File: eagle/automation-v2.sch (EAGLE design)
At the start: 103 parts, among them IC1 MEGA48/88/168-AU, IC2 DS2482-100S, IC3 DS2482-100S, IC4 78L33, K1 SRD-05VDC-SL-C, K2 SRD-05VDC-SL-C, K3 SRD-05VDC-SL-C, K4 SRD-05VDC-SL-C, Q1 BSS123, Q2 BSS123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

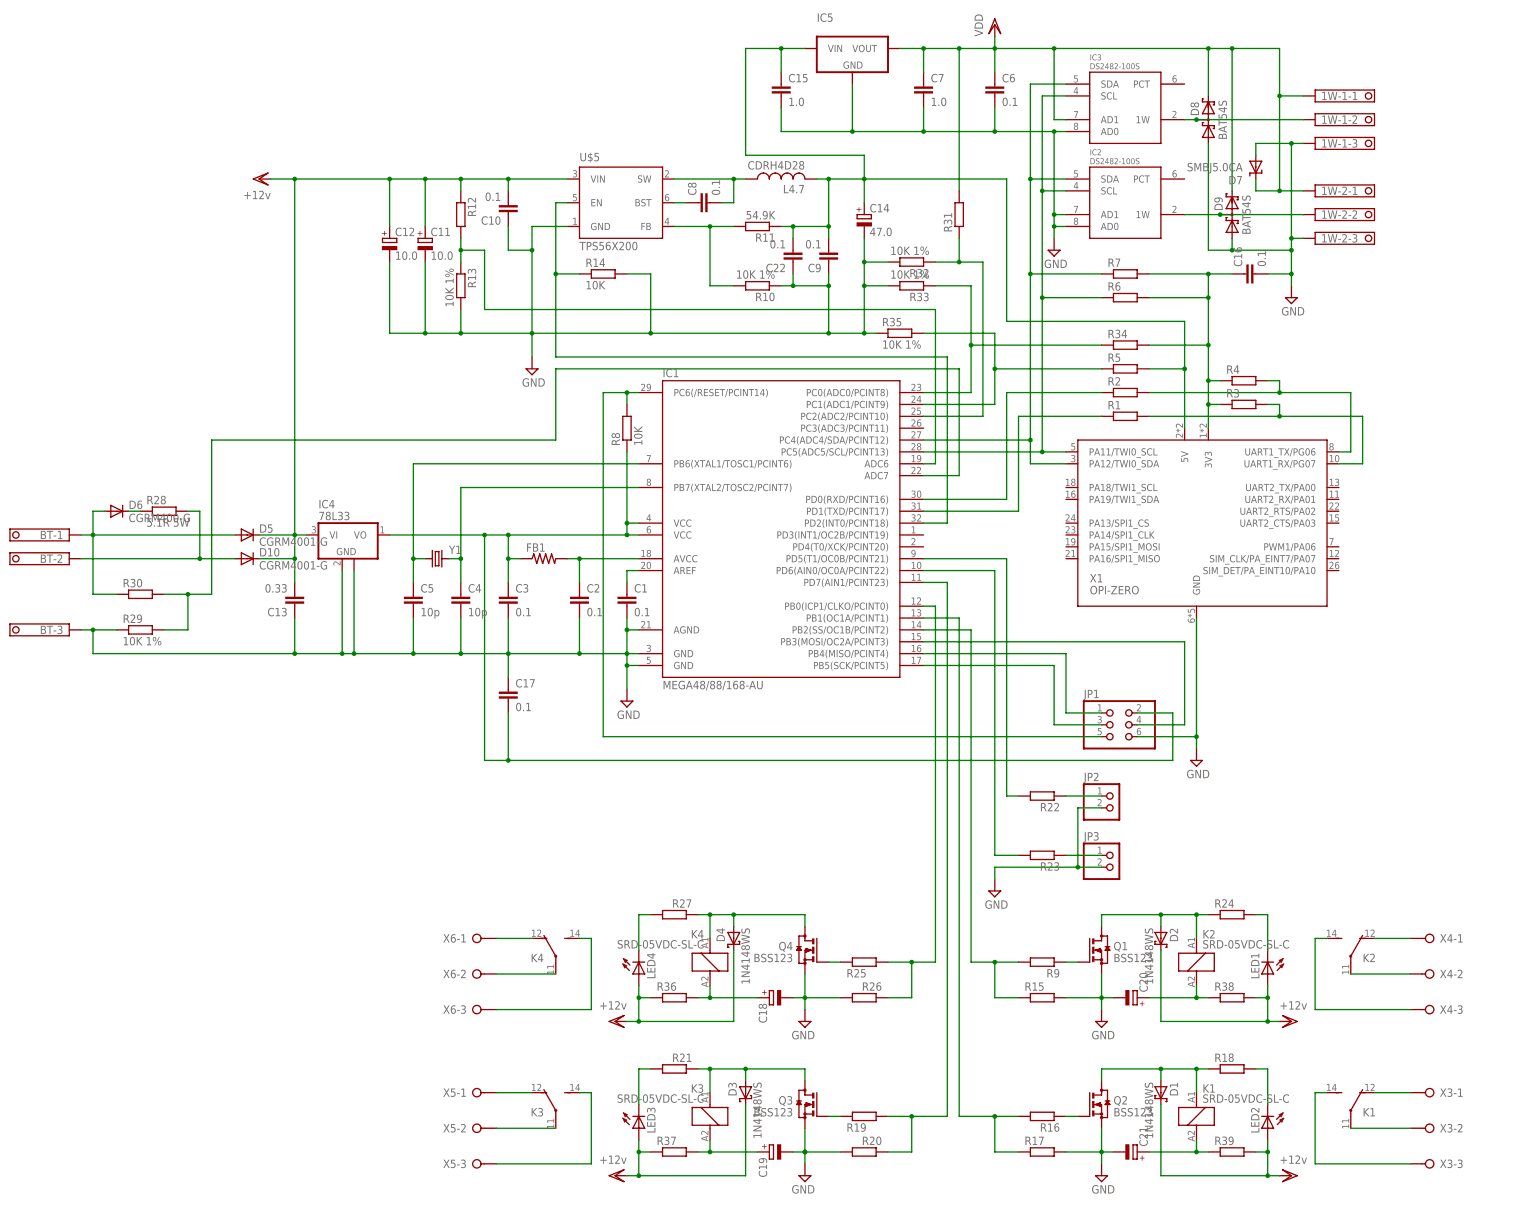
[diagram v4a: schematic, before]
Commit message: changed Relay footprint
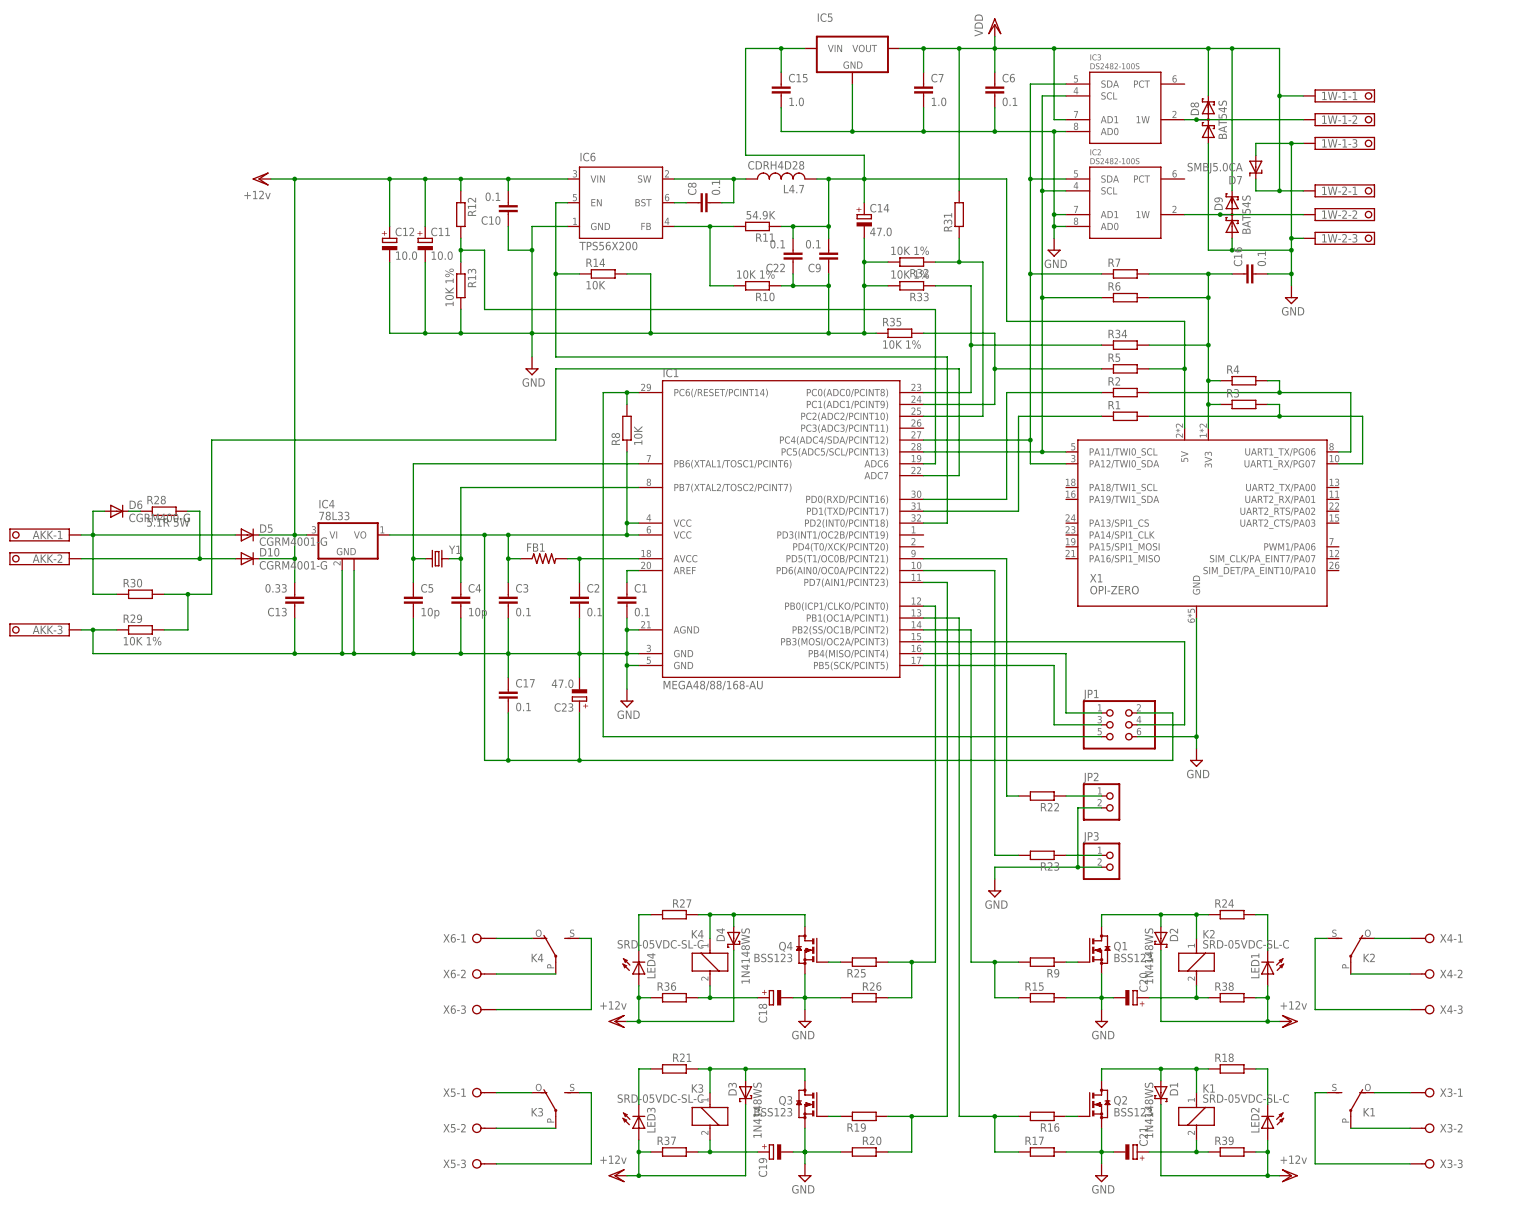
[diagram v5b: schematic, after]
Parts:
- added C23: 47.0, rcl:CPOL-EUB/3528-21R
- K1, K2, K3, K4: device relay:ZNS5106 -> relay:ZF112S
- renumbered BT to AKK, U$5 to IC6
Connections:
- net GND: now also C23.-
- net VCC: now also C23.+
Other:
- moved on the sheet: K1, K2, K3, K4
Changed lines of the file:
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@@
 <part name="C6" library="rcl" deviceset="C-EU" device="C0603" value="0.1"/>
 <part name="C7" library="rcl" deviceset="C-EU" device="C0805" value="1.0"/>
-<part name="U$5" library="custom" deviceset="TPS56X200" device=""/>
+<part name="IC6" library="custom" deviceset="TPS56X200" device=""/>
 <part name="U$6" library="USBug" deviceset="GND" device=""/>
 <part name="C8" library="rcl" deviceset="C-EU" device="C0805" value="0.1"/>
@@
 <part name="R15" library="rcl" deviceset="R-EU_" device="R0603"/>
 <part name="U$1" library="USBug" deviceset="GND" device=""/>
-<part name="K2" library="relay" deviceset="ZNS5*" device="" technology="106" value="SRD-05VDC-SL-C"/>
+<part name="K2" library="relay" deviceset="ZF112" device="S" value="SRD-05VDC-SL-C"/>
 <part name="JP2" library="pinhead" deviceset="PINHD-1X2" device=""/>
 <part name="JP3" library="pinhead" deviceset="PINHD-1X2" device=""/>
@@
 <part name="R17" library="rcl" deviceset="R-EU_" device="R0603"/>
 <part name="U$8" library="USBug" deviceset="GND" device=""/>
-<part name="K1" library="relay" deviceset="ZNS5*" device="" technology="106" value="SRD-05VDC-SL-C"/>
+<part name="K1" library="relay" deviceset="ZF112" device="S" value="SRD-05VDC-SL-C"/>
 <part name="D1" library="diode" deviceset="BAT60J" device="" value="1N4148WS"/>
 <part name="R18" library="rcl" deviceset="R-EU_" device="R0603"/>
@@
 <part name="R20" library="rcl" deviceset="R-EU_" device="R0603"/>
 <part name="U$9" library="USBug" deviceset="GND" device=""/>
-<part name="K3" library="relay" deviceset="ZNS5*" device="" technology="106" value="SRD-05VDC-SL-C"/>
+<part name="K3" library="relay" deviceset="ZF112" device="S" value="SRD-05VDC-SL-C"/>
 <part name="D3" library="diode" deviceset="BAT60J" device="" value="1N4148WS"/>
 <part name="R21" library="rcl" deviceset="R-EU_" device="R0603"/>
@@
 <part name="R26" library="rcl" deviceset="R-EU_" device="R0603"/>
 <part name="U$10" library="USBug" deviceset="GND" device=""/>
-<part name="K4" library="relay" deviceset="ZNS5*" device="" technology="106" value="SRD-05VDC-SL-C"/>
+<part name="K4" library="relay" deviceset="ZF112" device="S" value="SRD-05VDC-SL-C"/>
 <part name="D4" library="diode" deviceset="BAT60J" device="" value="1N4148WS"/>
 <part name="R27" library="rcl" deviceset="R-EU_" device="R0603"/>
@@
 <part name="V4" library="supply1" deviceset="VDD" device="" value="+12v"/>
 <part name="D5" library="diode" deviceset="CGRM400*-G" device="" technology="1"/>
-<part name="BT" library="con-phoenix-350" deviceset="1751251" device="" value=""/>
+<part name="AKK" library="con-phoenix-350" deviceset="1751251" device="" value=""/>
 <part name="D6" library="diode" deviceset="CGRM400*-G" device="" technology="1" value="CGRM400-G"/>
 <part name="R28" library="rcl" deviceset="R-EU_" device="VTA55" value="5.1R 5W"/>
@@
 <part name="X5" library="con-wago-508" deviceset="W237-03P" device=""/>
 <part name="X6" library="con-wago-508" deviceset="W237-03P" device=""/>
+<part name="C23" library="rcl" deviceset="CPOL-EU" device="B/3528-21R" value="47.0"/>
 </parts>
 <sheets>
@@
 <instance part="C6" gate="G$1" x="-27.94" y="142.24"/>
 <instance part="C7" gate="G$1" x="-43.18" y="142.24"/>
-<instance part="U$5" gate="G$1" x="-109.22" y="114.3"/>
+<instance part="IC6" gate="G$1" x="-109.22" y="114.3"/>
 <instance part="U$6" gate="G$2" x="-127" y="81.28"/>
 <instance part="C8" gate="G$1" x="-91.44" y="116.84" rot="R90"/>
@@
 <instance part="V4" gate="G$1" x="-109.22" y="-58.42" rot="MR270"/>
 <instance part="D5" gate="G$1" x="-187.96" y="45.72"/>
-<instance part="BT" gate="-1" x="-226.06" y="45.72" rot="R180"/>
-<instance part="BT" gate="-2" x="-226.06" y="40.64" rot="R180"/>
-<instance part="BT" gate="-3" x="-226.06" y="25.4" rot="R180"/>
+<instance part="AKK" gate="-1" x="-226.06" y="45.72" rot="R180"/>
+<instance part="AKK" gate="-2" x="-226.06" y="40.64" rot="R180"/>
+<instance part="AKK" gate="-3" x="-226.06" y="25.4" rot="R180"/>
 <instance part="D6" gate="G$1" x="-215.9" y="50.8"/>
 <instance part="R28" gate="G$1" x="-205.74" y="50.8"/>
@@
 <instance part="X6" gate="-2" x="-139.7" y="-48.26" rot="MR180"/>
 <instance part="X6" gate="-3" x="-139.7" y="-55.88" rot="MR180"/>
+<instance part="C23" gate="G$1" x="-116.84" y="10.16" rot="R180"/>
 </instances>
 <busses>
@@
 <pinref part="C17" gate="G$1" pin="1"/>
 <wire x1="-132.08" y1="15.24" x2="-132.08" y2="20.32" width="0.1524" layer="91"/>
-<pinref part="BT" gate="-3" pin="K"/>
+<pinref part="AKK" gate="-3" pin="K"/>
 <wire x1="-223.52" y1="25.4" x2="-220.98" y2="25.4" width="0.1524" layer="91"/>
 <junction x="-220.98" y="25.4"/>
+<pinref part="C23" gate="G$1" pin="-"/>
+<wire x1="-116.84" y1="15.24" x2="-116.84" y2="20.32" width="0.1524" layer="91"/>
 </segment>
 <segment>
@@
 </segment>
 <segment>
-<pinref part="U$5" gate="G$1" pin="GND"/>
+<pinref part="IC6" gate="G$1" pin="GND"/>
 <pinref part="U$6" gate="G$2" pin="GND"/>
 <wire x1="-119.38" y1="111.76" x2="-127" y2="111.76" width="0.1524" layer="91"/>
@@
 <wire x1="-137.16" y1="45.72" x2="-137.16" y2="-2.54" width="0.1524" layer="91"/>
 <wire x1="-137.16" y1="-2.54" x2="-132.08" y2="-2.54" width="0.1524" layer="91"/>
-<wire x1="-132.08" y1="-2.54" x2="10.16" y2="-2.54" width="0.1524" layer="91"/>
+<wire x1="-132.08" y1="-2.54" x2="-116.84" y2="-2.54" width="0.1524" layer="91"/>
+<wire x1="-116.84" y1="-2.54" x2="10.16" y2="-2.54" width="0.1524" layer="91"/>
 <wire x1="10.16" y1="-2.54" x2="10.16" y2="7.62" width="0.1524" layer="91"/>
 <pinref part="JP1" gate="A" pin="2"/>
@@
 <wire x1="-132.08" y1="7.62" x2="-132.08" y2="-2.54" width="0.1524" layer="91"/>
 <junction x="-132.08" y="-2.54"/>
+<pinref part="C23" gate="G$1" pin="+"/>
+<wire x1="-116.84" y1="7.62" x2="-116.84" y2="-2.54" width="0.1524" layer="91"/>
+<junction x="-116.84" y="-2.54"/>
 </segment>
 </net>
@@
 <net name="N$3" class="1">
 <segment>
-<pinref part="U$5" gate="G$1" pin="SW"/>
+<pinref part="IC6" gate="G$1" pin="SW"/>
 <wire x1="-96.52" y1="121.92" x2="-83.82" y2="121.92" width="0.1524" layer="91"/>
 <wire x1="-83.82" y1="121.92" x2="-83.82" y2="116.84" width="0.1524" layer="91"/>
@@
 <net name="N$17" class="0">
 <segment>
-<pinref part="U$5" gate="G$1" pin="BST"/>
+<pinref part="IC6" gate="G$1" pin="BST"/>
 <pinref part="C8" gate="G$1" pin="1"/>
 <wire x1="-96.52" y1="116.84" x2="-93.98" y2="116.84" width="0.1524" layer="91"/>
@@
 <net name="N$22" class="0">
 <segment>
-<pinref part="U$5" gate="G$1" pin="FB"/>
+<pinref part="IC6" gate="G$1" pin="FB"/>
 <pinref part="R11" gate="G$1" pin="2"/>
 <wire x1="-96.52" y1="111.76" x2="-88.9" y2="111.76" width="0.1524" layer="91"/>
@@
 <net name="N$27" class="0">
 <segment>
-<pinref part="U$5" gate="G$1" pin="EN"/>
+<pinref part="IC6" gate="G$1" pin="EN"/>
 <wire x1="-119.38" y1="116.84" x2="-121.92" y2="116.84" width="0.1524" layer="91"/>
 <wire x1="-121.92" y1="116.84" x2="-121.92" y2="101.6" width="0.1524" layer="91"/>
@@
 <net name="12V" class="1">
 <segment>
-<pinref part="U$5" gate="G$1" pin="VIN"/>
+<pinref part="IC6" gate="G$1" pin="VIN"/>
 <pinref part="C10" gate="G$1" pin="2"/>
 <wire x1="-119.38" y1="121.92" x2="-132.08" y2="121.92" width="0.1524" layer="91"/>
@@
 <wire x1="-215.9" y1="33.02" x2="-220.98" y2="33.02" width="0.1524" layer="91"/>
 <wire x1="-220.98" y1="33.02" x2="-220.98" y2="45.72" width="0.1524" layer="91"/>
-<pinref part="BT" gate="-1" pin="K"/>
+<pinref part="AKK" gate="-1" pin="K"/>
 <wire x1="-223.52" y1="45.72" x2="-220.98" y2="45.72" width="0.1524" layer="91"/>
 </segment>
@@
 <net name="N$31" class="1">
 <segment>
-<pinref part="BT" gate="-2" pin="K"/>
+<pinref part="AKK" gate="-2" pin="K"/>
 <wire x1="-223.52" y1="40.64" x2="-198.12" y2="40.64" width="0.1524" layer="91"/>
 <pinref part="R28" gate="G$1" pin="2"/>

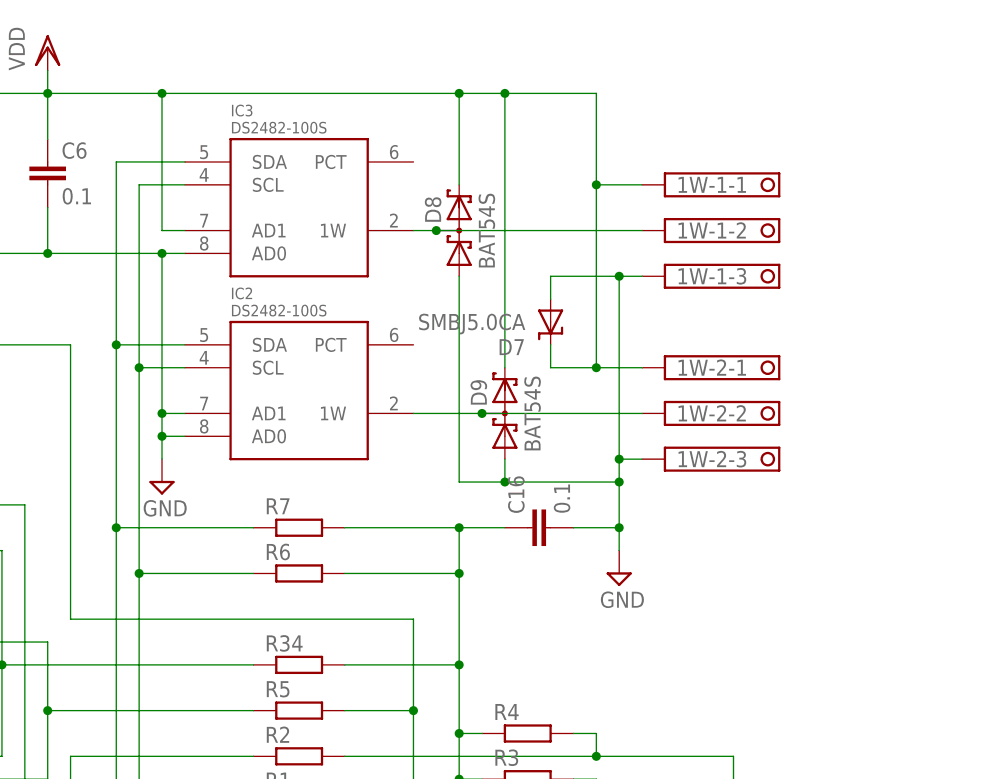
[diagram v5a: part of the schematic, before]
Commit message: strong 1w pullup added
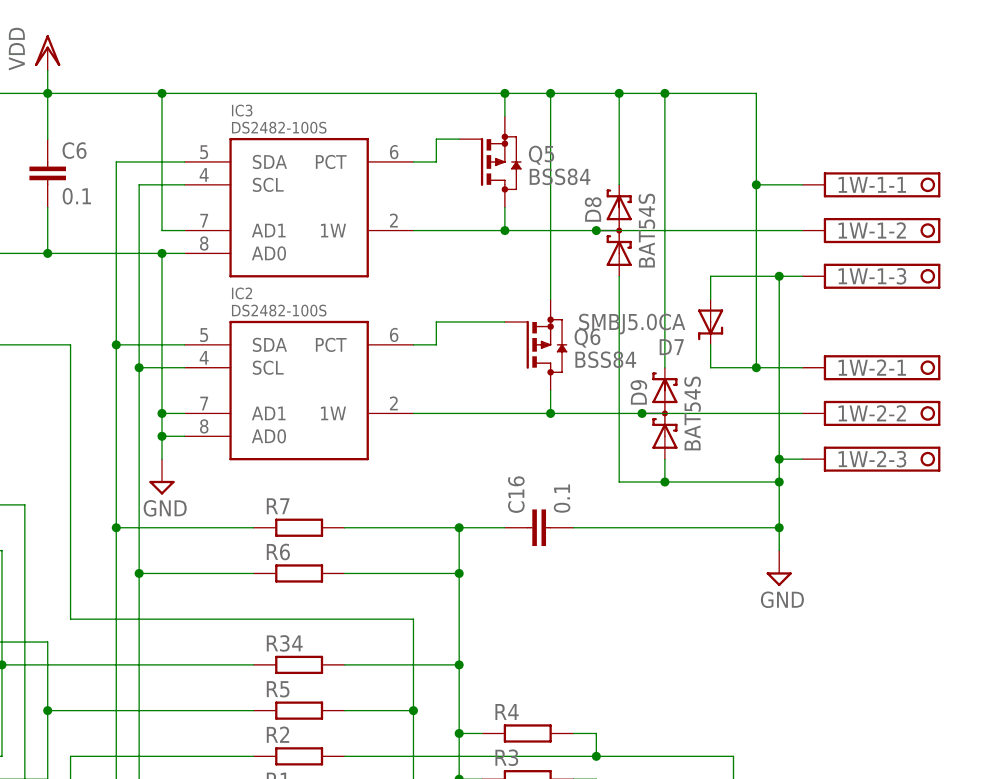
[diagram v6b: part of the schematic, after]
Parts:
- added Q5, Q6: BSS84, transistor-small-signal:BSS84
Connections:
- net N$1 renamed SDA
- net N$2 renamed SCL
- new net N$21: IC3G$1.PCT, Q5.G
- new net N$65: IC2G$1.PCT, Q6.G
- net N$30: now also Q5.D
- net N$60: now also Q6.D
- net VDD: now also Q5.S, Q6.S
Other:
- moved on the sheet: 1W-1-1, 1W-1-2, 1W-1-3, 1W-2-1, 1W-2-2, 1W-2-3, D7, D8, D9
